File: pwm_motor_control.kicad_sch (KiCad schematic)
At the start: 22 parts, among them Q1 NPN, U3 LTV-817S, U8 LM358, U9 LM358

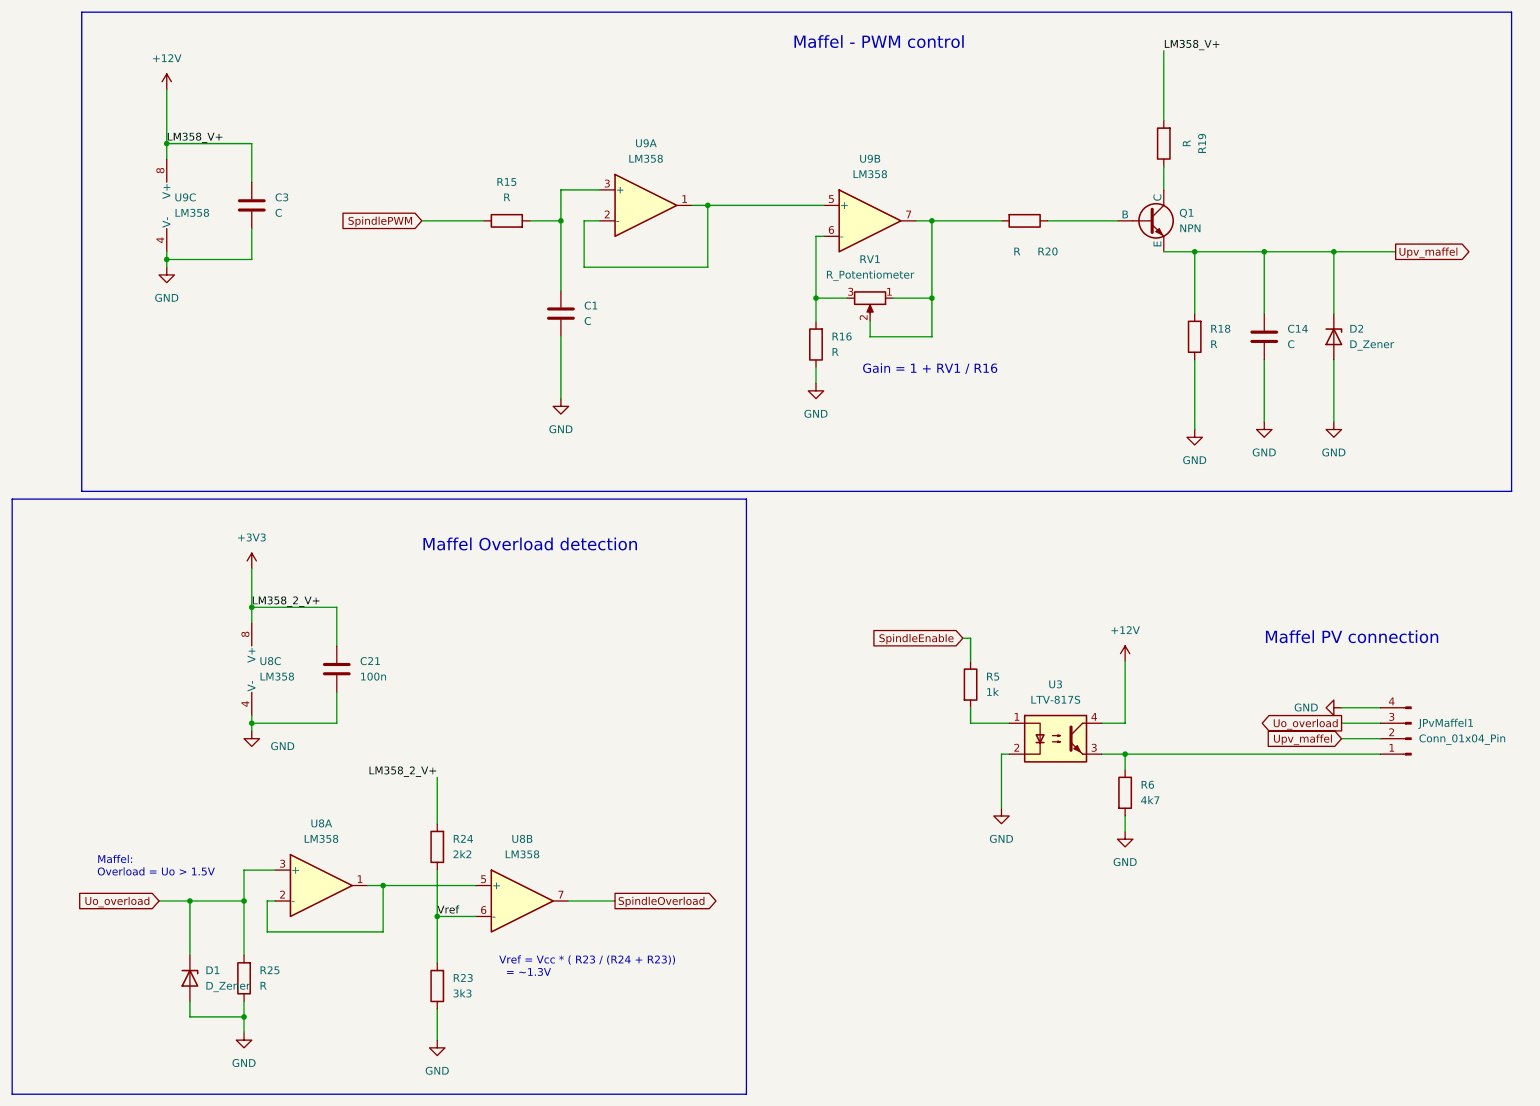
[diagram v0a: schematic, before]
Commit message: Version 1.1 - reworked all smd's to 0603
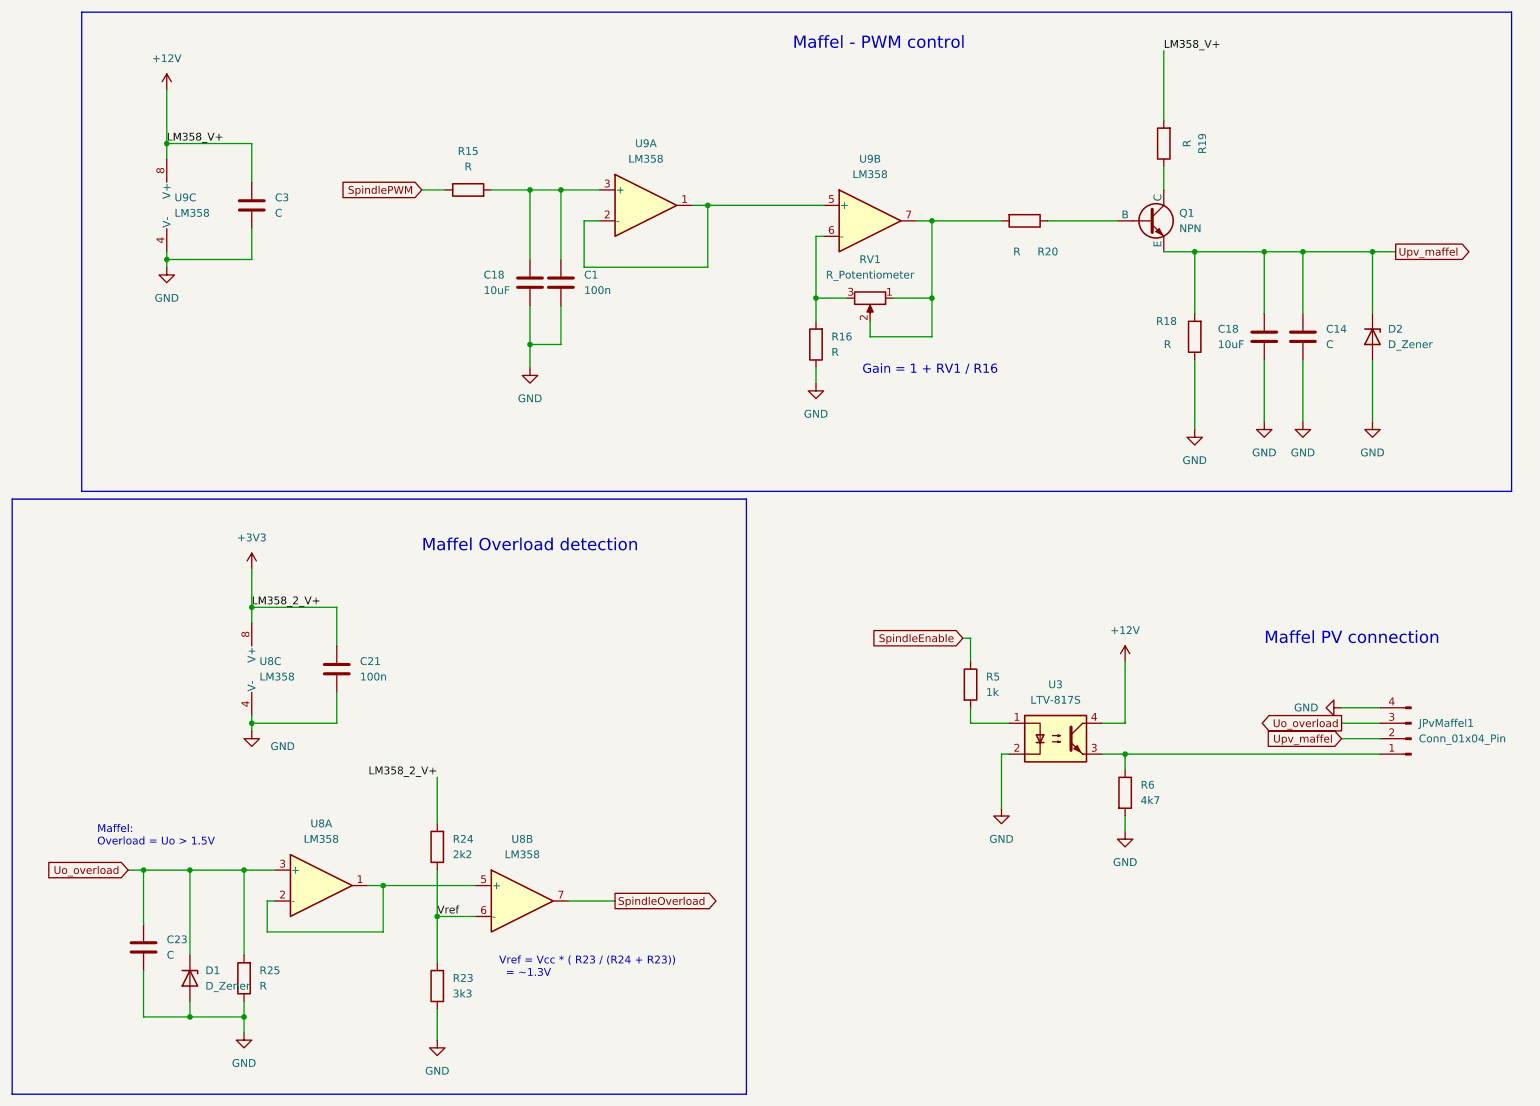
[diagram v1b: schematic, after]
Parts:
- added C18 (x2): 10uF, Inductor_SMD:L_1210_3225Metric_Pad1.42x2.65mm_HandSolder, symbol Device:C
- added C23: C, Capacitor_SMD:C_0603_1608Metric_Pad1.08x0.95mm_HandSolder, symbol Device:C
- C1: value C -> 100n; footprint Capacitor_SMD:C_0201_0603Metric_Pad0.64x0.40mm_HandSolder -> Capacitor_SMD:C_0603_1608Metric_Pad1.08x0.95mm_HandSolder
- C14, C21, C3: footprint Capacitor_SMD:C_0201_0603Metric_Pad0.64x0.40mm_HandSolder -> Capacitor_SMD:C_0603_1608Metric_Pad1.08x0.95mm_HandSolder
- R15, R16, R18, R19, R20, R23, R24, R25, R5, R6: footprint Resistor_SMD:R_0201_0603Metric_Pad0.64x0.40mm_HandSolder -> Resistor_SMD:R_0603_1608Metric_Pad0.98x0.95mm_HandSolder
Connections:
- net GND: now also C18.2, C18.2, C23.2
- net Uo_overload: now also C23.1
- net Upv_maffel: now also C18.1
- net at C1.1, R15.2, U9.3 (+): now also C18.1
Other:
- moved on the sheet: C14, D2, R15

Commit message: Updating 12V on/off with FET now; Laser connectors added
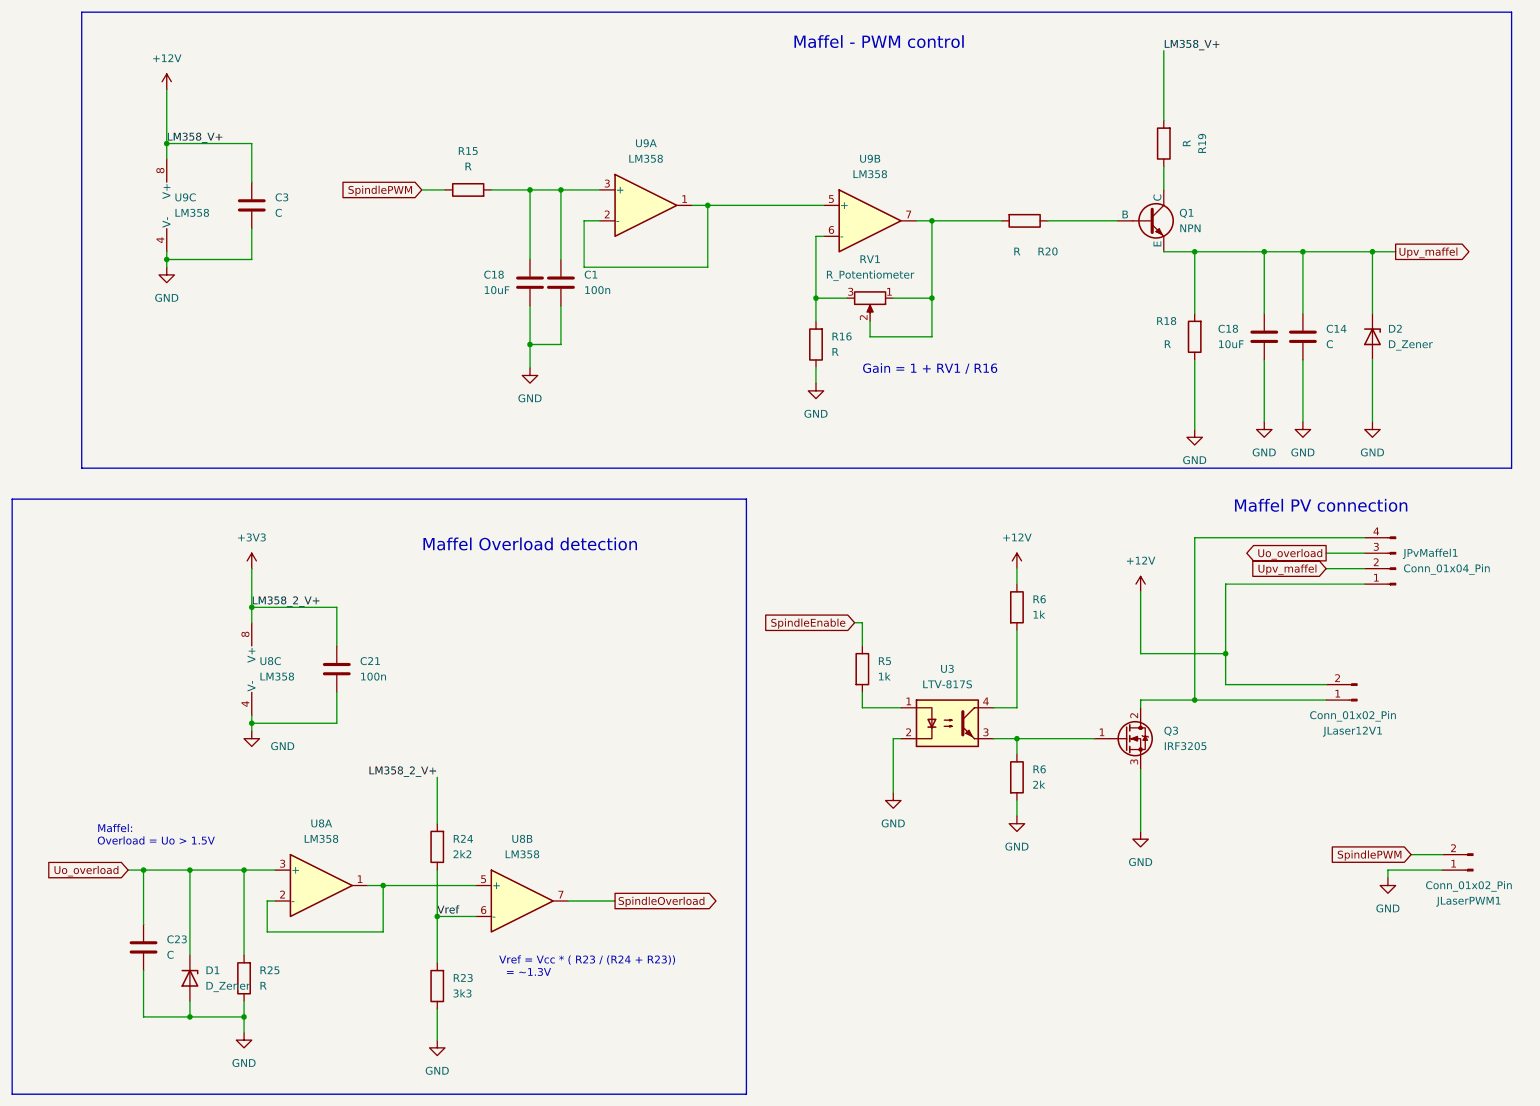
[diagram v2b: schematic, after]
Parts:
- added JLaser12V1, JLaserPWM1: Conn_01x02_Pin, Connector_PinHeader_2.54mm:PinHeader_1x02_P2.54mm_Vertical, symbol Connector:Conn_01x02_Pin
- added Q3: IRF3205, Package_TO_SOT_THT:TO-220-3_Vertical, symbol Transistor_FET:IRF3205
- added R6: 1k, Resistor_SMD:R_0603_1608Metric_Pad0.98x0.95mm_HandSolder, symbol Device:R
- R6: value 4k7 -> 2k
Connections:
- net +12V: now also JPvMaffel1.1 (Pin_1), JLaser12V1.2 (Pin_2), R6.1; no longer U3.4
- net GND: now also JLaserPWM1.1 (Pin_1), Q3.3 (S); no longer JPvMaffel1.4 (Pin_4)
- net SpindlePWM: now also JLaserPWM1.2 (Pin_2)
- net at R6.1, U3.3: now also Q3.1 (G); no longer JPvMaffel1.1 (Pin_1)
- new net: R6.2, U3.4
- new net: JLaser12V1.1 (Pin_1), JPvMaffel1.4 (Pin_4), Q3.2 (D)
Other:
- moved on the sheet: JPvMaffel1, R5, R6, U3

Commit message: Mainly value updates
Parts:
- C23: value C -> 10pf
- D1: value D_Zener -> 10V
- R15: value R -> 1k
- R16: value R -> 47k
- R25: value R -> 100k
- R5: value 1k -> 430
- RV1: value R_Potentiometer -> 100k
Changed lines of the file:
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@@
       (effects (font (size 1.27 1.27)) (justify right))
     )
-    (property "Value" "R" (at 58.42 173.99 0)
+    (property "Value" "100k" (at 58.42 173.99 0)
       (effects (font (size 1.27 1.27)) (justify right))
     )
@@
   )
   (symbol (lib_id "Device:C") (at 39.37 167.64 0) (unit 1)
-    (in_bom yes) (on_board yes) (dnp no) (fields_autoplaced)
-    (property "Reference" "C23" (at 43.18 166.37 0)
-      (effects (font (size 1.27 1.27)) (justify left))
-    )
-    (property "Value" "C" (at 43.18 168.91 0)
+    (in_bom yes) (on_board yes) (dnp no)
+    (property "Reference" "C23" (at 33.02 163.83 0)
+      (effects (font (size 1.27 1.27)) (justify left))
+    )
+    (property "Value" "10pf" (at 33.02 171.45 0)
       (effects (font (size 1.27 1.27)) (justify left))
     )
@@
       (effects (font (size 1.27 1.27)) (justify left))
     )
-    (property "Value" "D_Zener" (at 49.53 173.99 90)
+    (property "Value" "10V" (at 49.53 173.99 90)
       (effects (font (size 1.27 1.27)) (justify left))
     )
@@
       (effects (font (size 1.27 1.27)))
     )
-    (property "Value" "R_Potentiometer" (at 158.75 57.15 90)
+    (property "Value" "100k" (at 158.75 57.15 90)
       (effects (font (size 1.27 1.27)))
     )
@@
       (effects (font (size 1.27 1.27)))
     )
-    (property "Value" "R" (at 92.71 39.37 90)
+    (property "Value" "1k" (at 92.71 39.37 90)
       (effects (font (size 1.27 1.27)))
     )
@@
       (effects (font (size 1.27 1.27)) (justify right))
     )
-    (property "Value" "R" (at 152.4 69.85 0)
+    (property "Value" "47k" (at 152.4 69.85 0)
       (effects (font (size 1.27 1.27)) (justify right))
     )
@@
       (effects (font (size 1.27 1.27)) (justify left))
     )
-    (property "Value" "1k" (at 160.02 123.19 0)
-      (effects (font (size 1.27 1.27)) (justify left))
-    )
+    (property "Value" "430" (at 160.02 123.19 0)
+      (effects (font (size 1.27 1.27)) (justify left))
+    )
